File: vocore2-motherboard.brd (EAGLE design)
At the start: 100 x 100 mm, 93 parts, among them IC1 AP63205, IC2 FE1.1S, IC3 LM3671MF-3.3, IC4 LM3671MF-3.3, IC5 LM3671MF-3.3, IC6 FT232R, IC7 742G17DBV, J1 RJHSE-5381, J2 TE_1775470-8, J3 AMPHENOL_1140084168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

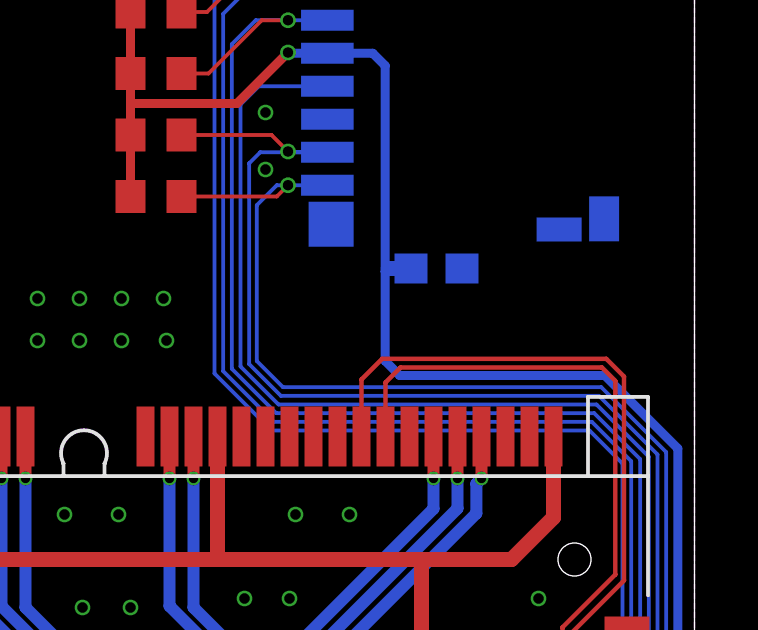
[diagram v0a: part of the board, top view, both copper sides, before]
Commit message: fix(p0led): use inverting-buffer to drive lan leds
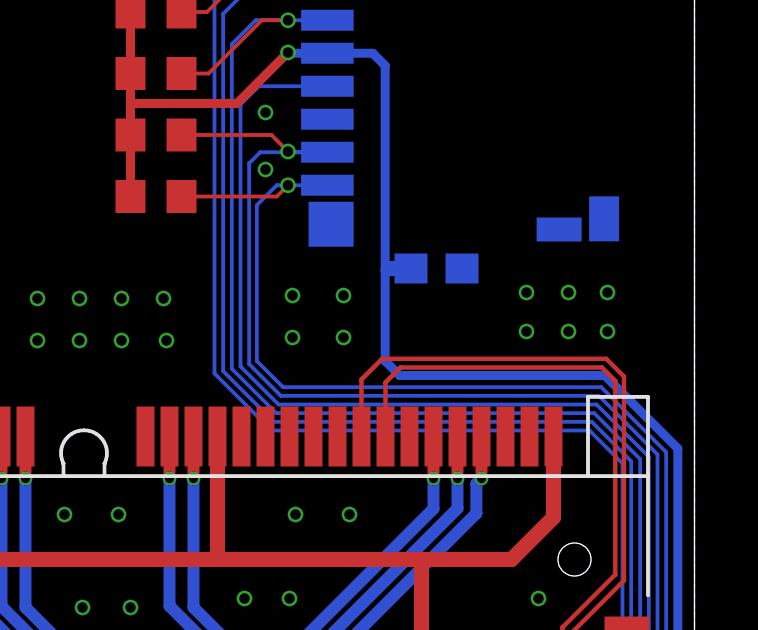
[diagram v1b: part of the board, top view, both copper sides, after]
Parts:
- IC7: value 742G17DBV -> SN74LVC2G14DBVR
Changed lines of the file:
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@@
 <element name="D3" library="diode" package="SMB" value="" x="-31.2" y="11.3" smashed="yes" rot="R270">
 <attribute name="FARNELL" value="1858651" x="-42.5" y="21.4" size="1.778" layer="27" rot="R270" display="off"/>
-<attribute name="MBM" value="1" x="-42.5" y="21.4" size="1.778" layer="27" rot="R270" display="off"/>
-<attribute name="PREIS" value="0,393" x="-42.5" y="21.4" size="1.778" layer="27" rot="R270" display="off"/>
+<attribute name="LCSC" value="C110478" x="-31.2" y="11.3" size="1.778" layer="27" rot="R270" display="off"/>
 <attribute name="VALUE" x="-34.629" y="13.459" size="1.27" layer="27" rot="R270"/>
 </element>
@@
 <element name="D2" library="diode" package="SMB" value="" x="-27.2" y="11.3" smashed="yes" rot="R270">
 <attribute name="FARNELL" value="1858651" x="-27.2" y="11.3" size="1.778" layer="27" rot="R270" display="off"/>
-<attribute name="MBM" value="1" x="-27.2" y="11.3" size="1.778" layer="27" rot="R270" display="off"/>
-<attribute name="PREIS" value="0,393" x="-27.2" y="11.3" size="1.778" layer="27" rot="R270" display="off"/>
+<attribute name="LCSC" value="C110478" x="-27.2" y="11.3" size="1.778" layer="27" rot="R270" display="off"/>
 <attribute name="VALUE" x="-30.629" y="13.459" size="1.27" layer="27" rot="R270"/>
 </element>
@@
 <attribute name="SPICEPREFIX" value="R" x="24.2" y="1.4" size="1.778" layer="27" rot="R180" display="off"/>
 </element>
-<element name="IC7" library="74xx-little-de" package="DBV_R-PDSO-G6" value="742G17DBV" x="28.8" y="2.45" smashed="yes" rot="R90">
-<attribute name="DIGIKEY" value="296-SN74LVC2G17DBVRCT-ND" x="28.8" y="2.45" size="1.778" layer="27" rot="R90" display="off"/>
-<attribute name="FARNELL" value="1470776" x="28.8" y="2.45" size="1.778" layer="27" rot="R90" display="off"/>
+<element name="IC7" library="74xx-little-de" package="DBV_R-PDSO-G6" value="SN74LVC2G14DBVR" x="28.8" y="2.45" smashed="yes" rot="R90">
+<attribute name="DIGIKEY" value="296-13010-1-ND" x="28.8" y="2.45" size="1.778" layer="27" rot="R90" display="off"/>
 </element>
 <element name="C25" library="rcl" library_urn="urn:adsk.eagle:library:334" package="C0603" package3d_urn="urn:adsk.eagle:package:23616/2" value="10uF" x="31.4" y="13.6" smashed="yes" rot="MR180">
@@
 <via x="12.6" y="26.1" extent="1-16" drill="0.35"/>
 <contactref element="C23" pad="2"/>
+<via x="36.6" y="56.8" extent="1-16" drill="0.35"/>
+<via x="38.3" y="56.8" extent="1-16" drill="0.35"/>
+<via x="36.6" y="55.4" extent="1-16" drill="0.35"/>
+<via x="38.3" y="55.4" extent="1-16" drill="0.35"/>
+<via x="44.4" y="56.9" extent="1-16" drill="0.35"/>
+<via x="45.8" y="56.9" extent="1-16" drill="0.35"/>
+<via x="47.1" y="56.9" extent="1-16" drill="0.35"/>
+<via x="44.4" y="55.6" extent="1-16" drill="0.35"/>
+<via x="45.8" y="55.6" extent="1-16" drill="0.35"/>
+<via x="47.1" y="55.6" extent="1-16" drill="0.35"/>
 </signal>
 <signal name="N$1">

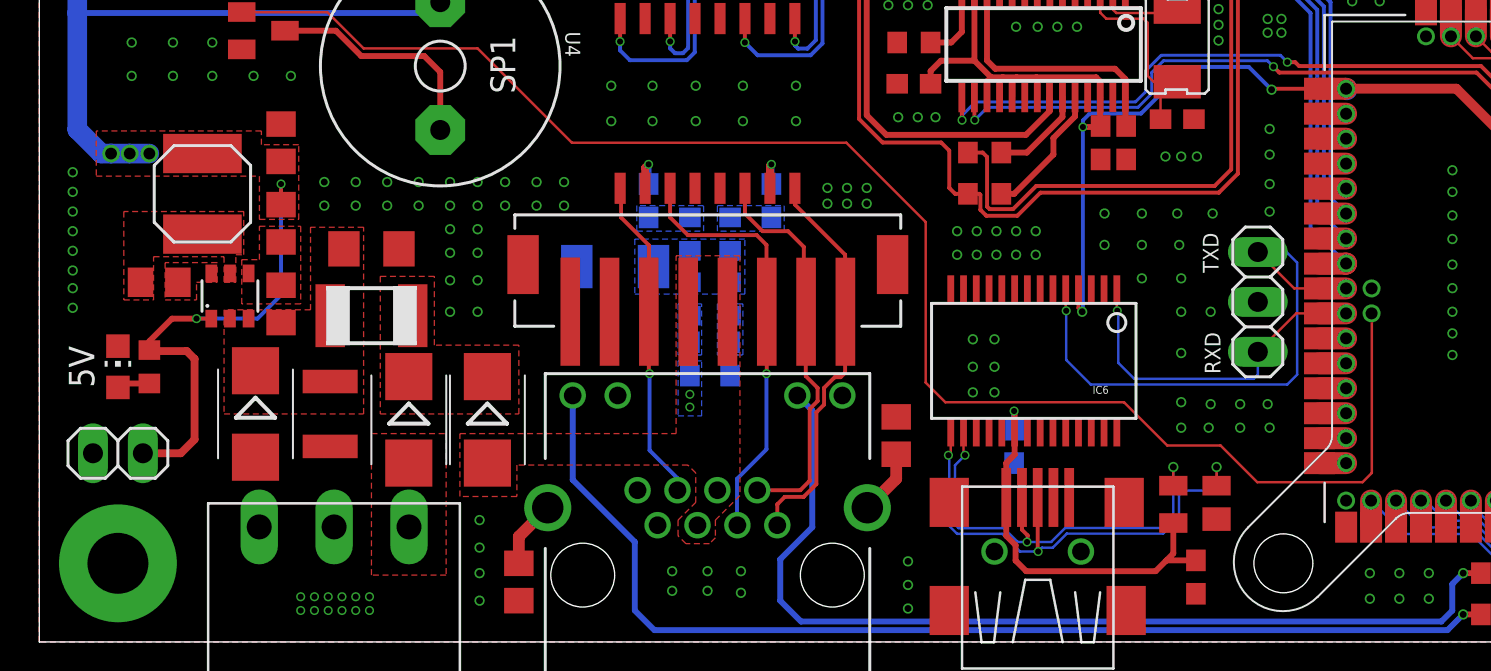
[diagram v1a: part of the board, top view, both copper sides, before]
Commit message: feat: use FT230X instead of FT232R
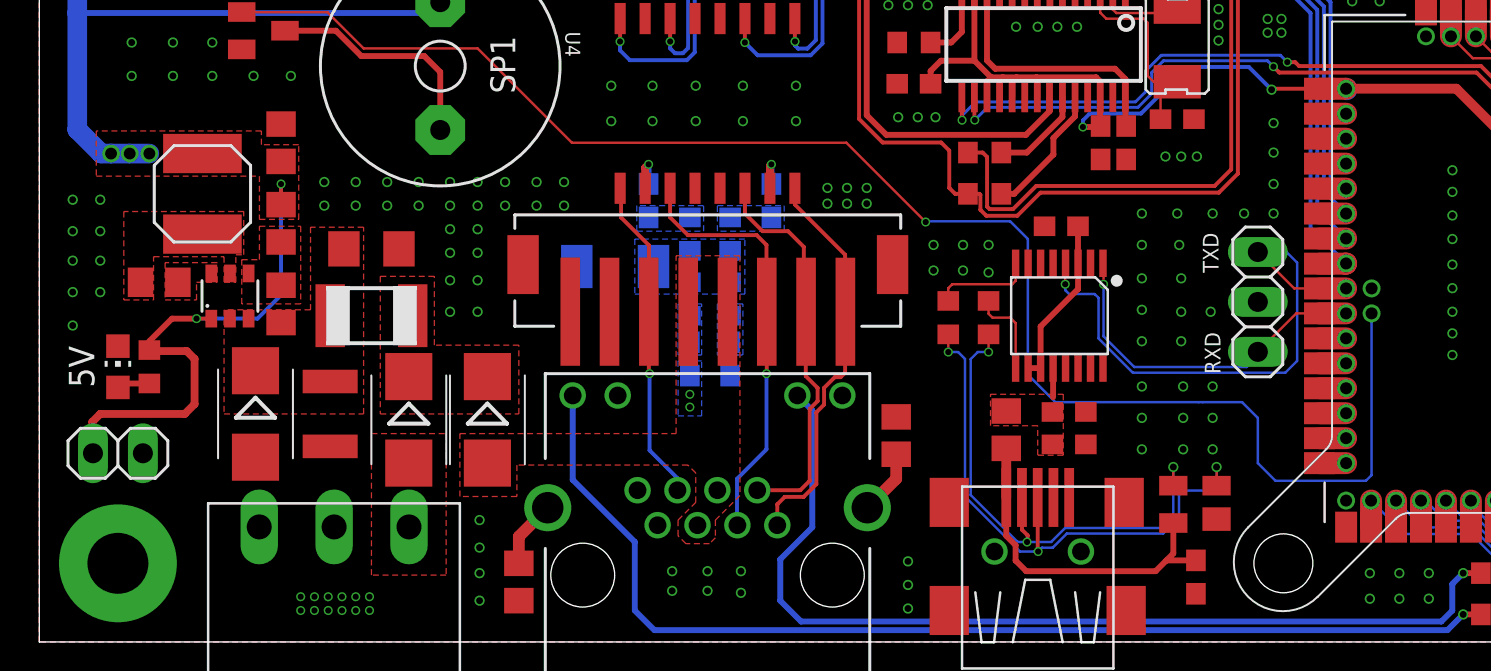
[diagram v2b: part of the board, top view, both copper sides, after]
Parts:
- removed C16: 100nF, rcl:C0603
- removed IC6: FT232R, SparkFun:SSOP28DB
- added C27, C29: 100nF, rcl:C0603
- added C28: 4.7uF, rcl:C0603
- added IC8: FT230XS-R, ftdi:SSOP16-0.635-5X4MM
- added L4: (no value), rcl:L0805
- added R20, R21: 27R, rcl:R0603
- turned JP7 to 0 degrees
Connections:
- new net FT230_VCCIO: C29.1, IC8.10, IC8.11, IC8.3
- new net N$35: C27.1, C28.1, IC8.12, L4.1
- new net N$36: IC8.9, R20.2
- new net N$38: IC8.8, R21.1
- net GND: now also C27.2, C28.2, C29.2, IC8.13, IC8.5; no longer C16.2, IC6.18, IC6.21, IC6.25, IC6.26, IC6.7
- net USB_D+: now also R21.2; no longer IC6.15
- net USB_D-: now also R20.1; no longer IC6.16
- net VC_3V3: no longer IC6.4
- net VOCORE_RXD2: now also IC8.1; no longer IC6.1
- net VOCORE_TXD2: now also IC8.4; no longer IC6.5
- net V_USB: now also L4.2; no longer C16.1, IC6.20
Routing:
- net VC_3V3: track 174.5 -> 163.9 mm, vias 5 -> 4
- net FT230_VCCIO: track 0.00 -> 8.64 mm
- net N$38: track 0.00 -> 5.12 mm
- net N$36: track 0.00 -> 4.51 mm
- net USB_D+: track 25.7 -> 29.6 mm
- net USB_D-: track 22.8 -> 26.6 mm
- net V_USB: track 20.6 -> 17.6 mm, vias 1 -> 0
- net +5V: track 250.1 -> 252.6 mm
- net N$35: track 0.00 -> 1.48 mm
- net VC_PWM1: track 80.5 -> 81.2 mm, vias 0 -> 1
- added copper zone on layer 1, net N$35

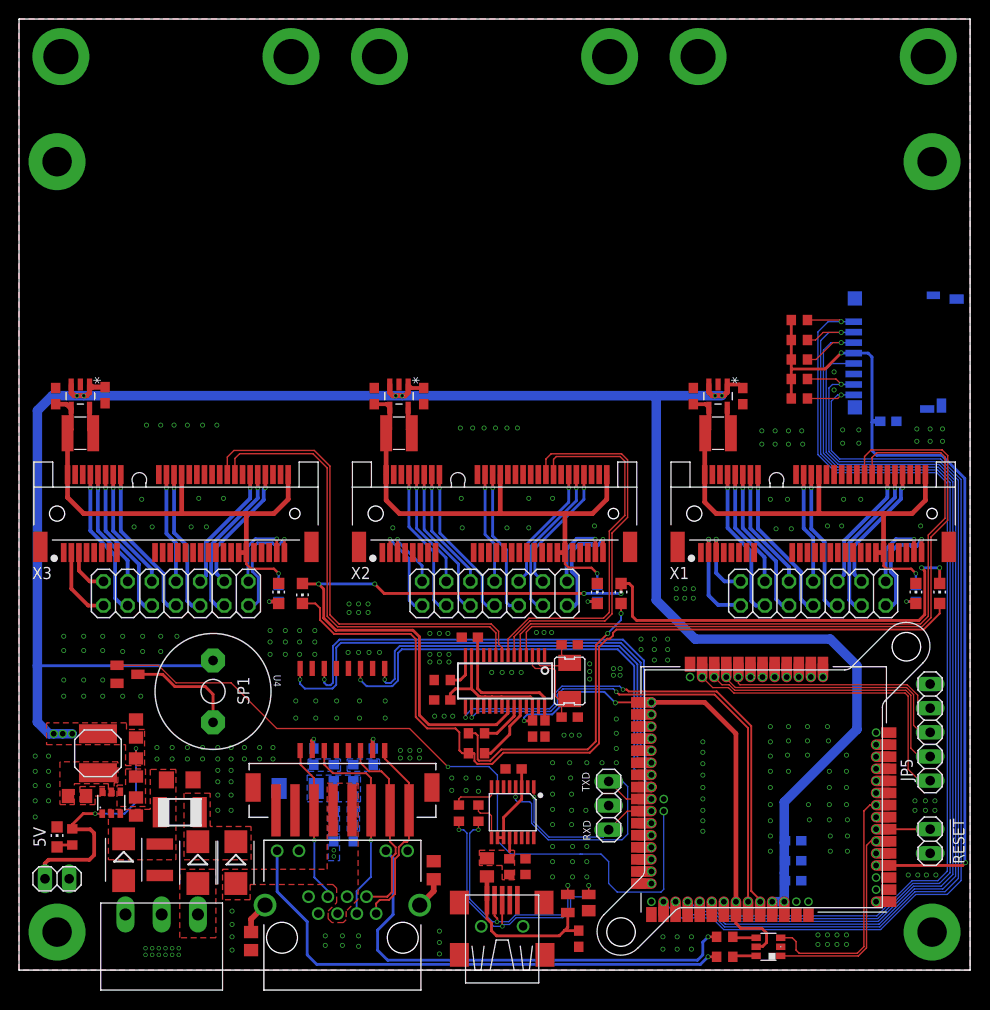
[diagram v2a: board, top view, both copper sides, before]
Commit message: feat(pcb): mounting hole for vocore
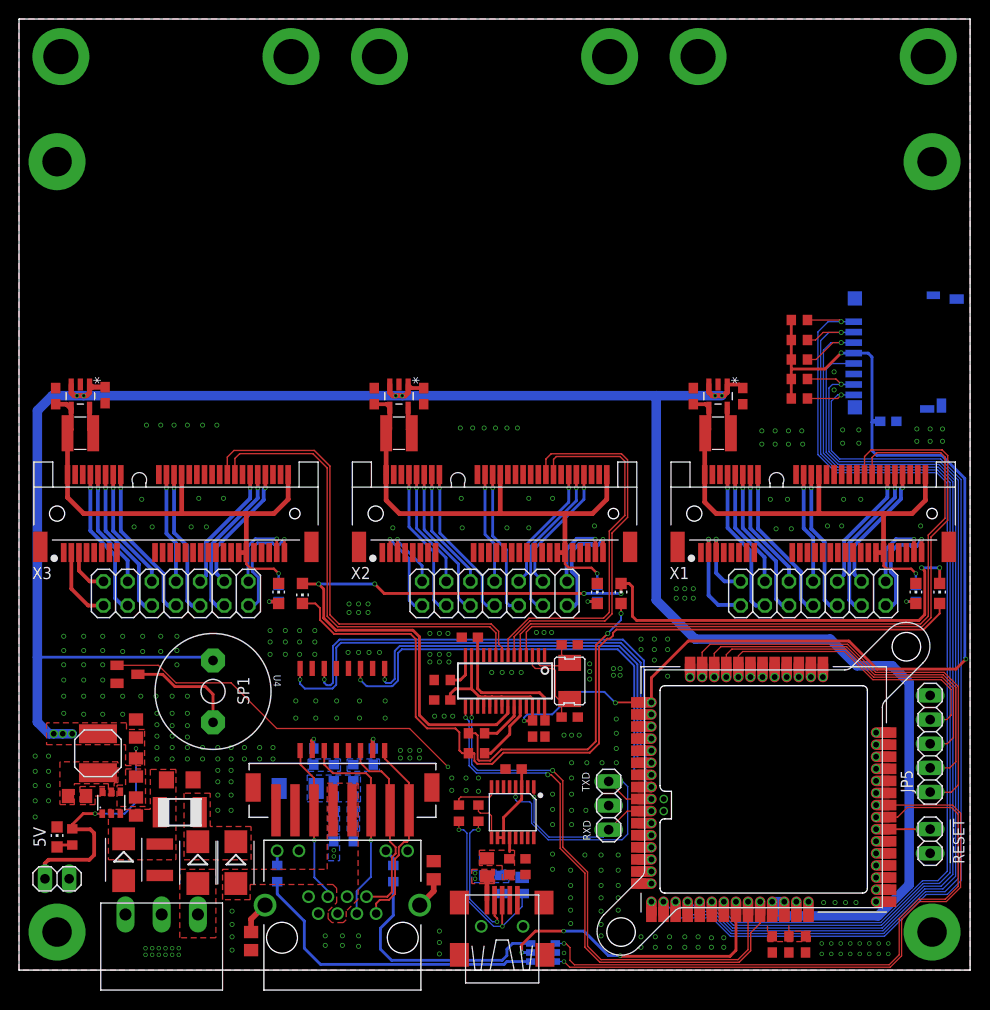
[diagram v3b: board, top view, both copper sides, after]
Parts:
- moved R15 47.9 mm to (-22.9, 10.2), flipped to the bottom, turned to 90 degrees
- moved R14 35.5 mm to (-10.7, 10.2), flipped to the bottom, turned to 90 degrees
- moved IC7 23.7 mm to (5.10, 1.85), flipped to the bottom, turned to 270 degrees
- moved C15 12.5 mm to (-1.15, 10.8), flipped to the bottom, turned to 90 degrees
- moved C25 11.1 mm to (29.2, 2.70), flipped to the top, turned to 270 degrees
- moved C19 8.81 mm to (30.9, 2.70), flipped to the top, turned to 270 degrees
- moved D4 7.28 mm to (1.80, 9.00), flipped to the bottom, turned to 270 degrees
- moved C17 6.82 mm to (32.7, 2.70), flipped to the top, turned to 270 degrees
- moved JP5 1.20 mm to (45.8, 23.8)
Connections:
- removed net N$46: U1.142_1, U1.142_2
- removed net N$67: IC7.4, R14.1
- new net N$35165: U1.137_1, U1.137_2
- new net N$37: IC7.4, R15.1
- net LED_LAN_LNK: now also U1.142_1, U1.142_2; no longer U1.137_1, U1.137_2
- net N$66: now also R14.1; no longer R15.1
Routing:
- net N$41: track 56.0 -> 1.54 mm, vias 1 -> 0
- net N$42: track 49.3 -> 1.86 mm, vias 1 -> 0
- net LED_LAN_LNK: track 22.7 -> 68.0 mm, vias 0 -> 1
- net VC_PWM1: track 81.2 -> 39.4 mm
- net LED_LAN_ACT: track 27.4 -> 67.0 mm, vias 0 -> 1
- net N$37: track 0.00 -> 32.8 mm
- net N$66: track 2.49 -> 25.1 mm
- net +5V: track 252.6 -> 269.9 mm
- net V_USB: track 17.6 -> 2.50 mm, vias 0 -> 2
- net VC_SPI_CS0: track 34.3 -> 46.7 mm
- net USB_D-: track 26.6 -> 15.1 mm, vias 3 -> 2
- net VC_SPI_CLK: track 30.8 -> 42.1 mm
- net VC_SPI_MISO: track 27.7 -> 37.4 mm
- net GND: track 0.00 -> 9.44 mm, vias 316 -> 315
- net VC_SPI_MOSI: track 23.8 -> 32.9 mm
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- added copper zone on layer 1, net V_USB
- added copper zone on layer 16, net V_USB
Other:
- outline, holes or cut-outs redrawn

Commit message: fix(brd): proper heatsink dimensions
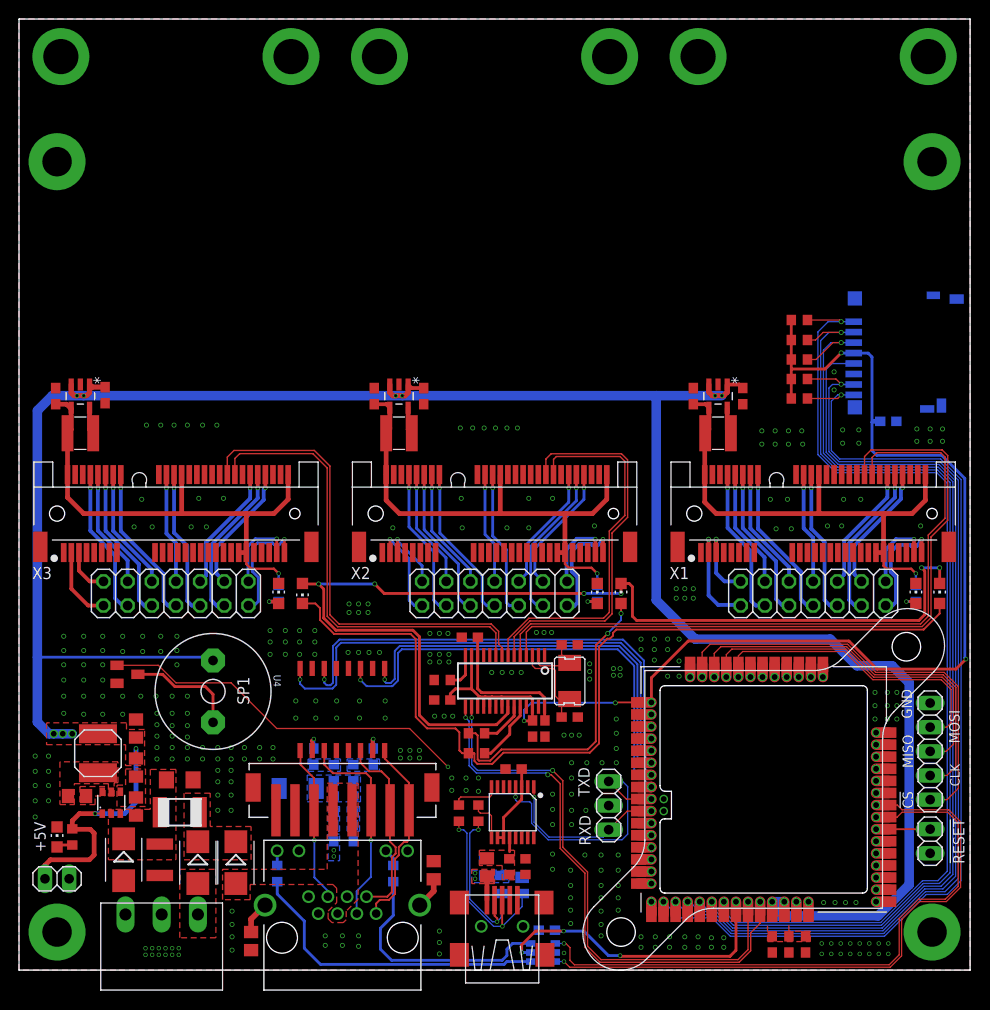
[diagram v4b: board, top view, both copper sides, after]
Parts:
- added C16: 100nF, rcl:C0603
- moved JP5 0.80 mm to (45.8, 23.0)
- turned U$1 to 0 degrees
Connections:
- net GND: now also C16.2
- net VC_3V3: now also C16.1
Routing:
- net USB_D-: track 15.1 -> 18.3 mm
- net LED_LAN_ACT: track 67.0 -> 65.1 mm
- net LED_LAN_LNK: track 68.0 -> 67.1 mm
- net VC_SPI_MOSI: track 32.9 -> 33.7 mm
- net VC_SPI_MISO: track 37.4 -> 38.2 mm
- net VC_SPI_CLK: track 42.1 -> 42.7 mm
- net VC_SPI_CS0: track 46.7 -> 47.2 mm
- net GND: vias 315 -> 327
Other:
- board text added: "!CS"
- board text added: "+5V"
- board text added: "CLK"
- board text added: "GND"
- board text added: "MISO"
- board text added: "MOSI"
- board text removed: "5V"
